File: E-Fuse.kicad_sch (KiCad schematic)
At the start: 4 parts, among them U4 TPS16630PWPR

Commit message: resistor values
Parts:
- R_ILIM: Digikey (none) -> RMCF0805FT3K00CT-ND; MPN (none) -> RMCF0805FT3K00; Manufacturer (none) -> Stackpole Electronics Inc
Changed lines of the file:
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@@
+			)
+		)
+		(property "Digikey" "RMCF0805FT3K00CT-ND"
+			(at 170.18 114.3 0)
+			(hide yes)
+			(show_name no)
+			(do_not_autoplace no)
+			(effects
+				(font
+					(size 1.27 1.27)
+				)
+			)
+		)
+		(property "MPN" "RMCF0805FT3K00"
+			(at 170.18 114.3 0)
+			(hide yes)
+			(show_name no)
+			(do_not_autoplace no)
+			(effects
+				(font
+					(size 1.27 1.27)
+				)
+			)
+		)
+		(property "Manufacturer" "Stackpole Electronics Inc"
+			(at 170.18 114.3 0)
+			(hide yes)
+			(show_name no)
+			(do_not_autoplace no)
+			(effects
+				(font
+					(size 1.27 1.27)
+				)
 			)
 		)

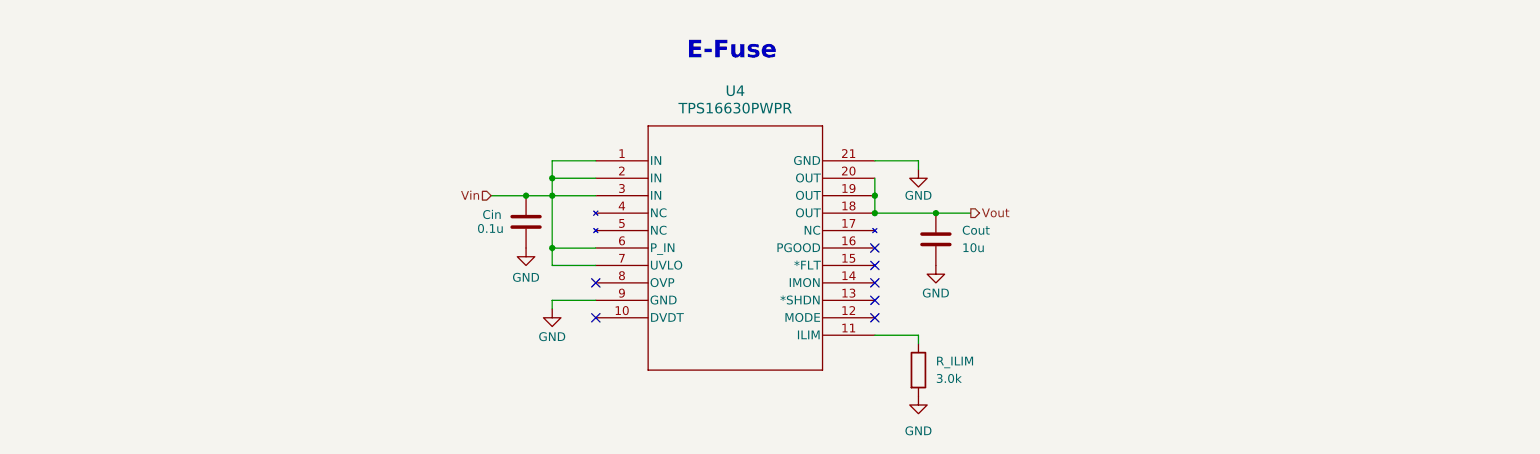
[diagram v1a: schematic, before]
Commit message: updates to BOM and power connections
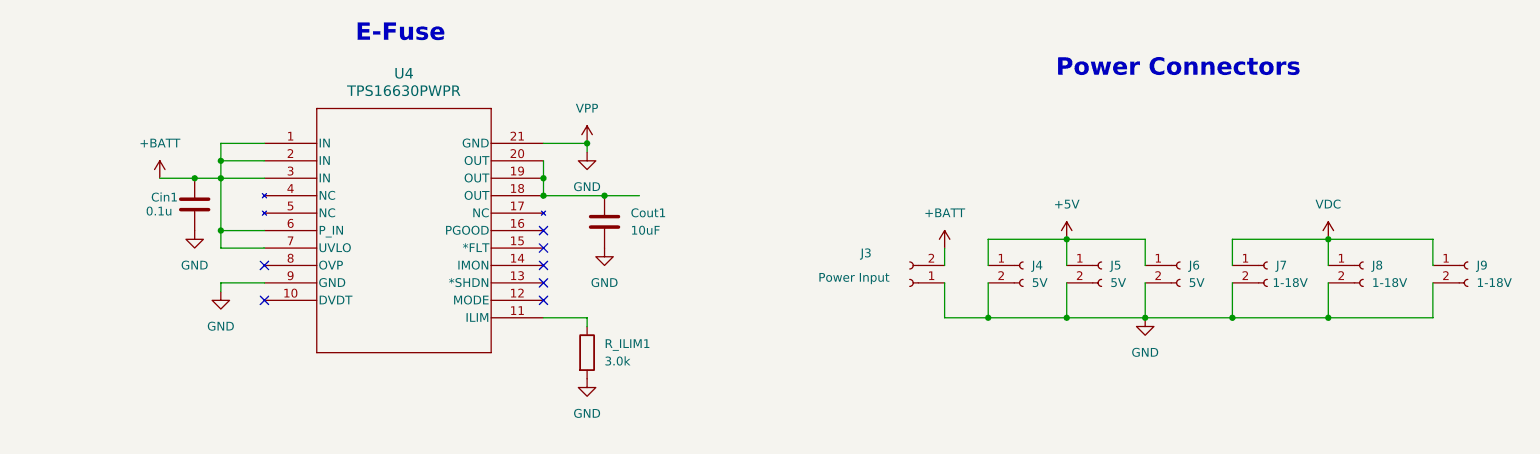
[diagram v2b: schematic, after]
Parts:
- added J3: Power Input, symbol Connector:Conn_01x02_Socket
- added J4, J5, J6: 5V, Connector_JST:JST_XH_S2B-XH-A_1x02_P2.50mm_Horizontal, symbol Connector:Conn_01x02_Socket
- added J7, J8, J9: 1-18V, Connector_JST:JST_XH_S2B-XH-A_1x02_P2.50mm_Horizontal, symbol Connector:Conn_01x02_Socket
- Cin1: renamed from Cin; footprint (none) -> Capacitor_SMD:C_0805_2012Metric
- Cout1: renamed from Cout; value 10u -> 10uF; footprint (none) -> Capacitor_SMD:C_0805_2012Metric
- R_ILIM1: renamed from R_ILIM; footprint (none) -> Resistor_SMD:R_0805_2012Metric
- U4: footprint HTSSOP20_PWP_TEX -> LEOS:HTSSOP20_PWP_TEX; Digikey (none) -> 296-TPS16630PWPRCT-ND; MPN (none) -> TPS16630PWPR; Manufacturer (none) -> Texas Instruments
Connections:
- net GND: now also J3.1 (Pin_1), J4.2 (Pin_2), J5.2 (Pin_2), J6.2 (Pin_2), J7.2 (Pin_2), J8.2 (Pin_2), J9.2 (Pin_2)
- net Vin renamed +BATT
- net +BATT: now also J3.2 (Pin_2)
- net Vout: no longer names the net of Cout1.1, U4.18 (OUT), U4.19 (OUT), U4.20 (OUT)
- new net +5V: J4.1 (Pin_1), J5.1 (Pin_1), J6.1 (Pin_1)
- new net VDC: J7.1 (Pin_1), J8.1 (Pin_1), J9.1 (Pin_1)
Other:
- note added: "Power Connectors"
- title: (none) -> E-Fuse
- moved on the sheet: Cin1, Cout1, R_ILIM1, U4

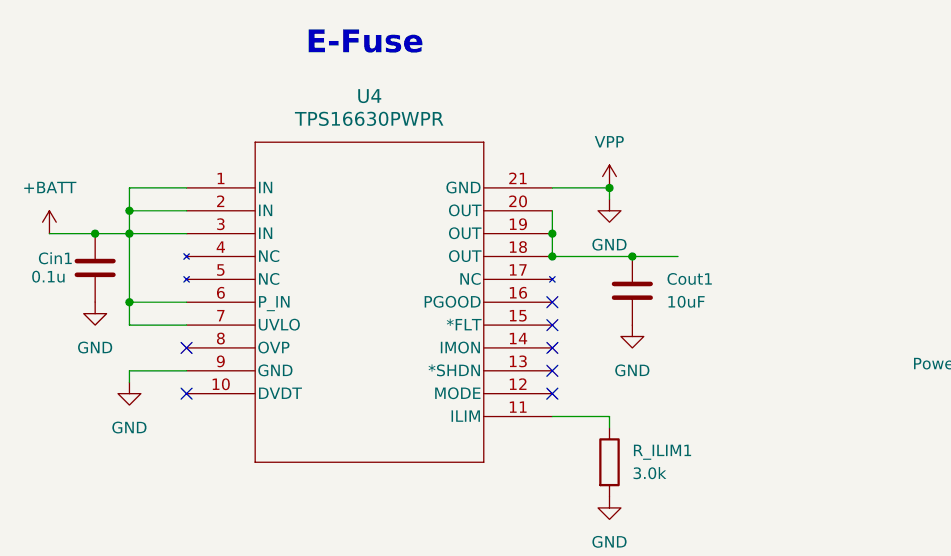
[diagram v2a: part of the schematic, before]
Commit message: updates to BOM and fixes for ERC
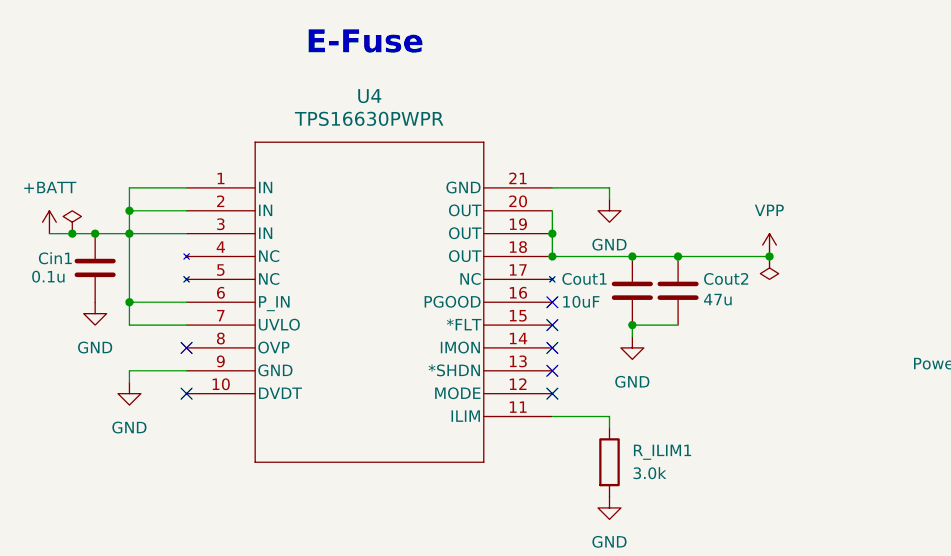
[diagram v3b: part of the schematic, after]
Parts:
- added Cout2: 47u, Capacitor_SMD:C_1206_3216Metric, symbol Device:C
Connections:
- net GND: now also Cout2.2
- net VPP: now reaches Cout1.1, U4.18 (OUT), U4.19 (OUT), U4.20 (OUT)
- net VPP: now also Cout2.1

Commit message: updates to efuse
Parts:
- added CdVdt: 4.7n, Capacitor_SMD:C_0805_2012Metric, symbol Device:C
- added Cin2: 10uF, Capacitor_SMD:C_0805_2012Metric, symbol Device:C
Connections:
- net +BATT: now also Cin2.1
- net GND: now also U4.8 (OVP), CdVdt.2, Cin2.2
- net at U4.10 (DVDT): now also CdVdt.1
- no-connect marks 7 -> 5
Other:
- moved on the sheet: Cin1

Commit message: updates to BOM and beginning of routing
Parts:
- added TP5, TP6: TestPoint, TestPoint:TestPoint_Loop_D2.60mm_Drill0.9mm_Beaded, symbol Connector:TestPoint
- J3: footprint (none) -> Connector_AMASS:AMASS_XT60IPW-M_1x03_P7.20mm_Horizontal; Manufacturer (none) -> JST
- J4, J5, J6, J7, J8, J9: Digikey (none) -> 455-S2B-XH-A-ND; MPN (none) -> S2B-XH-A; Manufacturer (none) -> JST
- renumbered CdVdt to CdVdt1
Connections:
- net +BATT: no longer U4.7 (UVLO)
- net GND: now also TP6.1
- net VDC: now also TP5.1

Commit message: updates to BOM
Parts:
- added R.1: 150k, Resistor_THT:R_Axial_DIN0207_L6.3mm_D2.5mm_P10.16mm_Horizontal, symbol Device:R
- added R.2: 10k, Resistor_THT:R_Axial_DIN0207_L6.3mm_D2.5mm_P10.16mm_Horizontal, symbol Device:R
- added TPUVLO: TestPoint, TestPoint:TestPoint_Loop_D2.60mm_Drill0.9mm_Beaded, symbol Connector:TestPoint
- Cout2: value 47u -> 10uF; footprint Capacitor_SMD:C_1206_3216Metric -> Capacitor_SMD:C_0805_2012Metric; Digikey 4713-GMC31X5R476M25NTCT-ND -> 1276-6698-1-ND; MPN GMC31X5R476M25NT -> CL21X106KAYNNNE; Manufacturer Cal-Chip Electronics, Inc. -> Samsung Electro-Mechanics
- TPGND2: renamed from TP6; value TestPoint -> GND TestPoint; Digikey (none) -> 36-5001-ND; MPN (none) -> 5001; Manufacturer (none) -> Keystone Electronics
- U4: Digikey 296-TPS16630PWPRCT-ND -> 296-TPS16630PWPTCT-ND; MPN TPS16630PWPR -> TPS16630PWPT
- renumbered TP5 to TP1-18V
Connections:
- net +BATT: now also R.1.1
- net GND: now also R.2.2
- net at U4.7 (UVLO): now also R.1.2, R.2.1, TPUVLO.1
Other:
- note added: "R_ILIM1 current limit 6A"
- note added: "UVLO resistors chosen for 6s Lipo Battery, through-hole 19V cutoff"
- moved on the sheet: Cin1, Cin2

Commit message: switching frequency
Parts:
- renumbered TP1-18V to TP1-18, TPUVLO to TPUVLO1
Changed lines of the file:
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@@
 		(in_pos_files yes)
 		(dnp no)
-		(property "Reference" "TP1-18V"
+		(property "Reference" "TP1-18"
 			(at 243.586 89.916 0)
 			(show_name no)
@@
 			(project "LEOS-F26-power"
 				(path "/3703ddf2-8141-438d-86a8-1eaec9672d0d/470843d4-556c-4e78-8e6c-25b65a02e4d0"
-					(reference "TP1-18V")
+					(reference "TP1-18")
 					(unit 1)
 				)
@@
 		(in_pos_files yes)
 		(dnp no)
-		(property "Reference" "TPUVLO"
+		(property "Reference" "TPUVLO1"
 			(at 60.198 94.742 90)
 			(show_name no)
@@
 			(project "LEOS-F26-power"
 				(path "/3703ddf2-8141-438d-86a8-1eaec9672d0d/470843d4-556c-4e78-8e6c-25b65a02e4d0"
-					(reference "TPUVLO")
-					(unit 1)
-				)
+					(reference "TPUVLO1")
+					(unit 1)
+				)
